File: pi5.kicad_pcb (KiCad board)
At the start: 2 copper layers, 319 parts, among them J1 USB_C_Receptacle_GCT_USB4105-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, J10 RJ45_Wuerth_7499111446_Horizo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, J11 USB_A_Wuerth_61400826021_Hori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, J12 USB3_A_Molex_48406-0001_Horiz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, J13 HDMI_Micro-D_Molex_46765-1xxx, J14 PinHeader_2x02_P2.54mm_Vertic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, J17 JST_SH_BM04B-SRSS-TB_1x04-1MP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, J2 HDMI_Micro-D_Molex_46765-1xxx, J20 52559-1652, J3 F32Q-1A7H1-11022, J4 F32Q-1A7H1-11022, J8 PinHeader_2x20_P2.54mm_Vertic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, J9 104031-0811, U5 DA9091

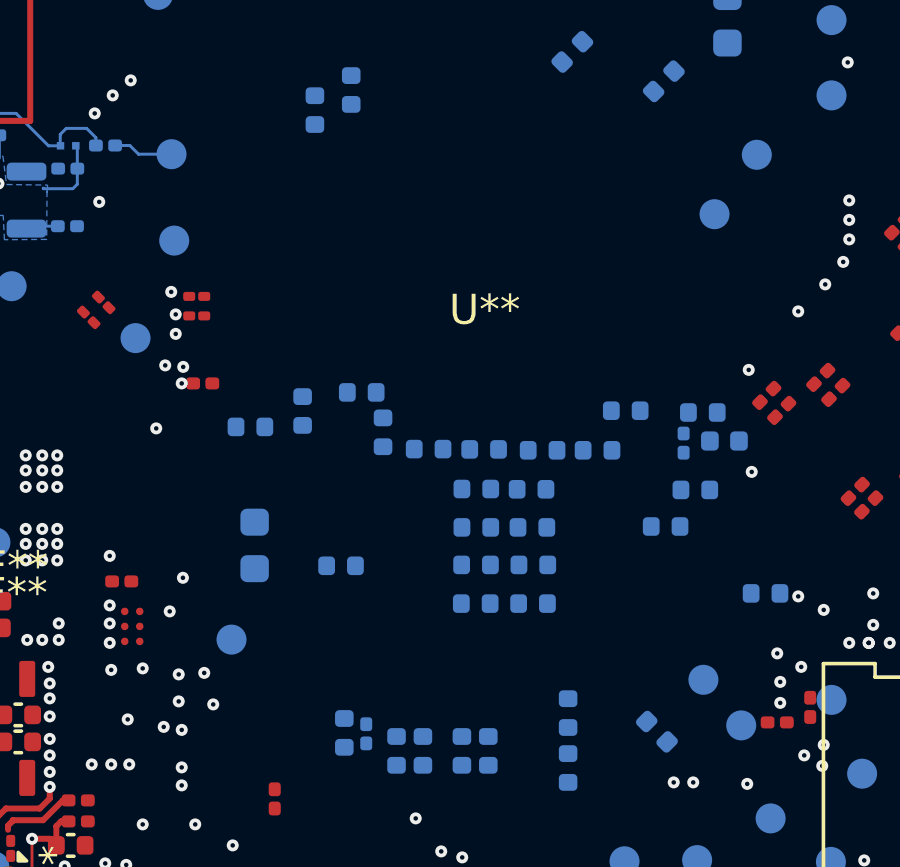
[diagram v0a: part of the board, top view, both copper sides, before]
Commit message: new component identifications
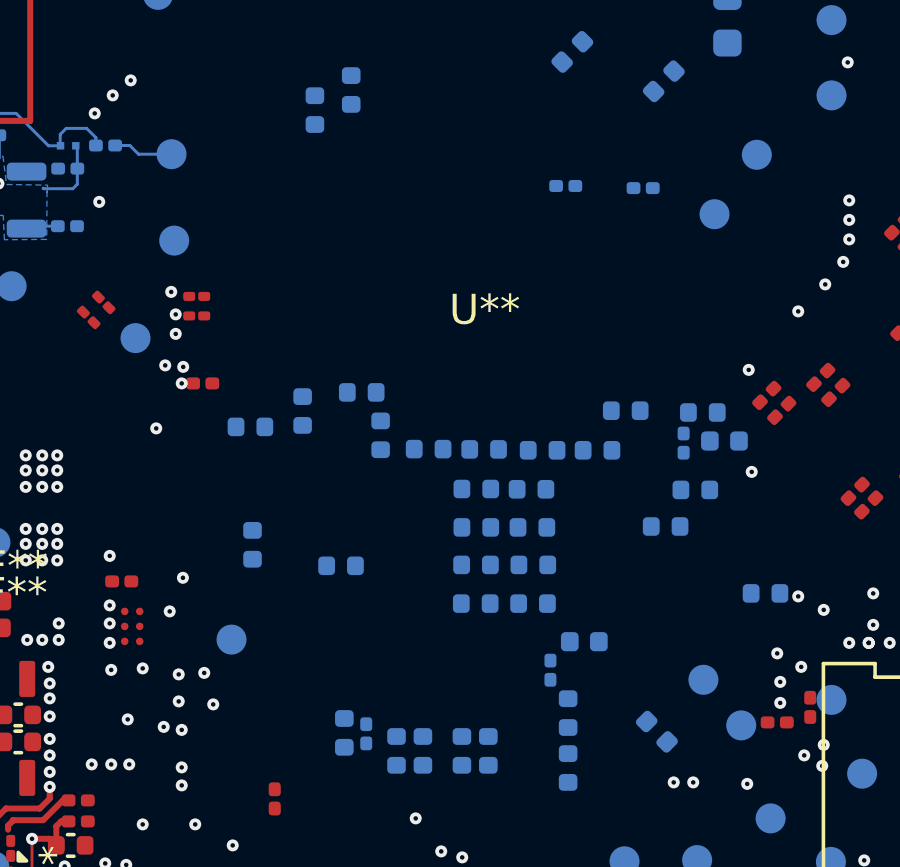
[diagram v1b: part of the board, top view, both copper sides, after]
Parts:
- added REF**: L_0402_1005Metric, Inductor_SMD:L_0402_1005Metric, B.Cu at (133.0, 102.8)
- added REF**: 10n, Capacitor_SMD:C_0201_0603Metric, B.Cu at (131.8, 103.7)
- added REF**: 100n, Capacitor_SMD:C_0201_0603Metric, B.Cu at (134.9, 87.6)
- added REF**: 100n, Capacitor_SMD:C_0201_0603Metric, B.Cu at (132.3, 87.6)
- REF**: value C_0603_1608Metric -> 4u7; footprint Capacitor_SMD:C_0603_1608Metric -> Capacitor_SMD:C_0402_1005Metric
- REF** (x2): value C_0402_1005Metric -> 15u
- moved REF** 0.13 mm to (126.2, 95.9)
- moved REF** 0.07 mm to (121.9, 99.5)
